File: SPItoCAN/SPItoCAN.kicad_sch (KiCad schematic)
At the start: 16 parts, among them J1 CONN_01x02, J2 CONN_01x02, J3 CONN_01x02, J4 Conn_01x07, U1 TJA1051T-E, U2 MCP2515-xSO, Y1 Crystal_8MHz

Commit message: Cleaned up PCB layout, added ground plane
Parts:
- added TP1, TP10, TP11, TP12, TP13, TP2, TP3, TP4, TP5, TP6, TP7, TP8, TP9: Test_Point_SMD, TestPoint:TestPoint_Pad_D1.5mm, symbol baja_schematics:Test_Point_SMD
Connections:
- net CANH: now also TP2.1
- net CANL: now also TP1.1
- net CS: now also TP10.1
- net GND: now also C3.2, C4.2, C5.2, D1.1 (K), TP13.1
- net INT: now also TP5.1
- net RXCAN: now also TP4.1
- net SCK: now also TP8.1
- net SI: now also TP9.1
- net SO: now also TP11.1
- net TXCAN: now also TP3.1
- net VCC: now also TP12.1; no longer C3.2, C4.2, C5.2, D1.1 (K)
- net OSC1 renamed OSC+
- net OSC+: now also TP7.1
- net OSC2 renamed OSC-
- net OSC-: now also TP6.1

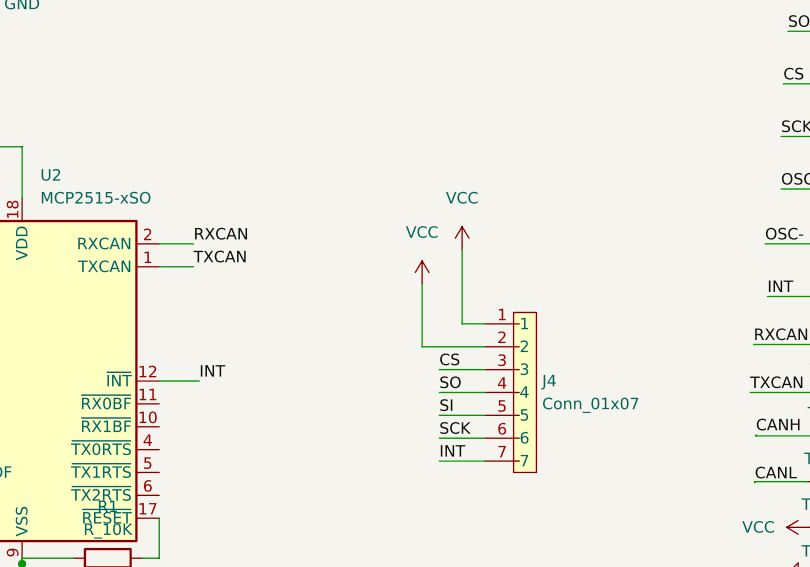
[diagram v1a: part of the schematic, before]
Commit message: cleaned up pcb, improved silkscreen, ran test gerber export
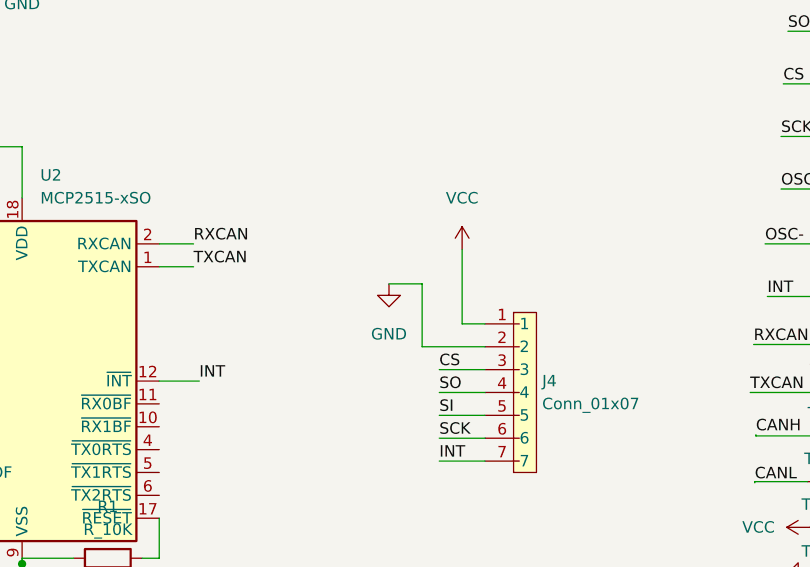
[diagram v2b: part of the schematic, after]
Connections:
- net GND: now also J4.2
- net VCC: no longer J4.2
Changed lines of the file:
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@@
+    (stroke (width 0) (type default) (color 0 0 0 0))
+  )
+  (wire (pts (xy 113.157 83.185) (xy 116.84 83.185))
     (stroke (width 0) (type default) (color 0 0 0 0))
   )
@@
     (pin "1")
   )
-  (symbol (lib_id "power:VCC") (at 116.84 83.185 0) (unit 1)
-    (in_bom yes) (on_board yes) (fields_autoplaced)
-    (property "Reference" "#PWR0104" (id 0) (at 116.84 86.995 0)
-      (effects (font (size 1.27 1.27)) hide)
-    )
-    (property "Value" "VCC" (id 1) (at 116.84 77.47 0))
-    (property "Footprint" "" (id 2) (at 116.84 83.185 0)
-      (effects (font (size 1.27 1.27)) hide)
-    )
-    (property "Datasheet" "" (id 3) (at 116.84 83.185 0)
-      (effects (font (size 1.27 1.27)) hide)
-    )
-    (pin "1")
-  )
   (symbol (lib_id "power:VCC") (at 67.945 119.38 0) (unit 1)
     (in_bom yes) (on_board yes)
@@
     )
     (property "Datasheet" "" (id 3) (at 161.29 100.076 0)
+      (effects (font (size 1.27 1.27)) hide)
+    )
+    (pin "1")
+  )
+  (symbol (lib_id "power:GND") (at 113.157 83.185 0) (unit 1)
+    (in_bom yes) (on_board yes) (fields_autoplaced)
+    (property "Reference" "#PWR0104" (id 0) (at 113.157 89.535 0)
+      (effects (font (size 1.27 1.27)) hide)
+    )
+    (property "Value" "GND" (id 1) (at 113.157 88.773 0))
+    (property "Footprint" "" (id 2) (at 113.157 83.185 0)
+      (effects (font (size 1.27 1.27)) hide)
+    )
+    (property "Datasheet" "" (id 3) (at 113.157 83.185 0)
       (effects (font (size 1.27 1.27)) hide)
     )
@@
       (reference "#PWR0103") (unit 1) (value "VCC") (footprint "")
     )
-    (path "/49441612-08d3-4f3e-a0e3-e44a83005088"
-      (reference "#PWR0104") (unit 1) (value "VCC") (footprint "")
+    (path "/7b13cfce-7857-47fb-8497-9e34fe39cc9c"
+      (reference "#PWR0104") (unit 1) (value "GND") (footprint "")
     )
     (path "/97c46783-6240-4233-9319-22c43f9f5727"

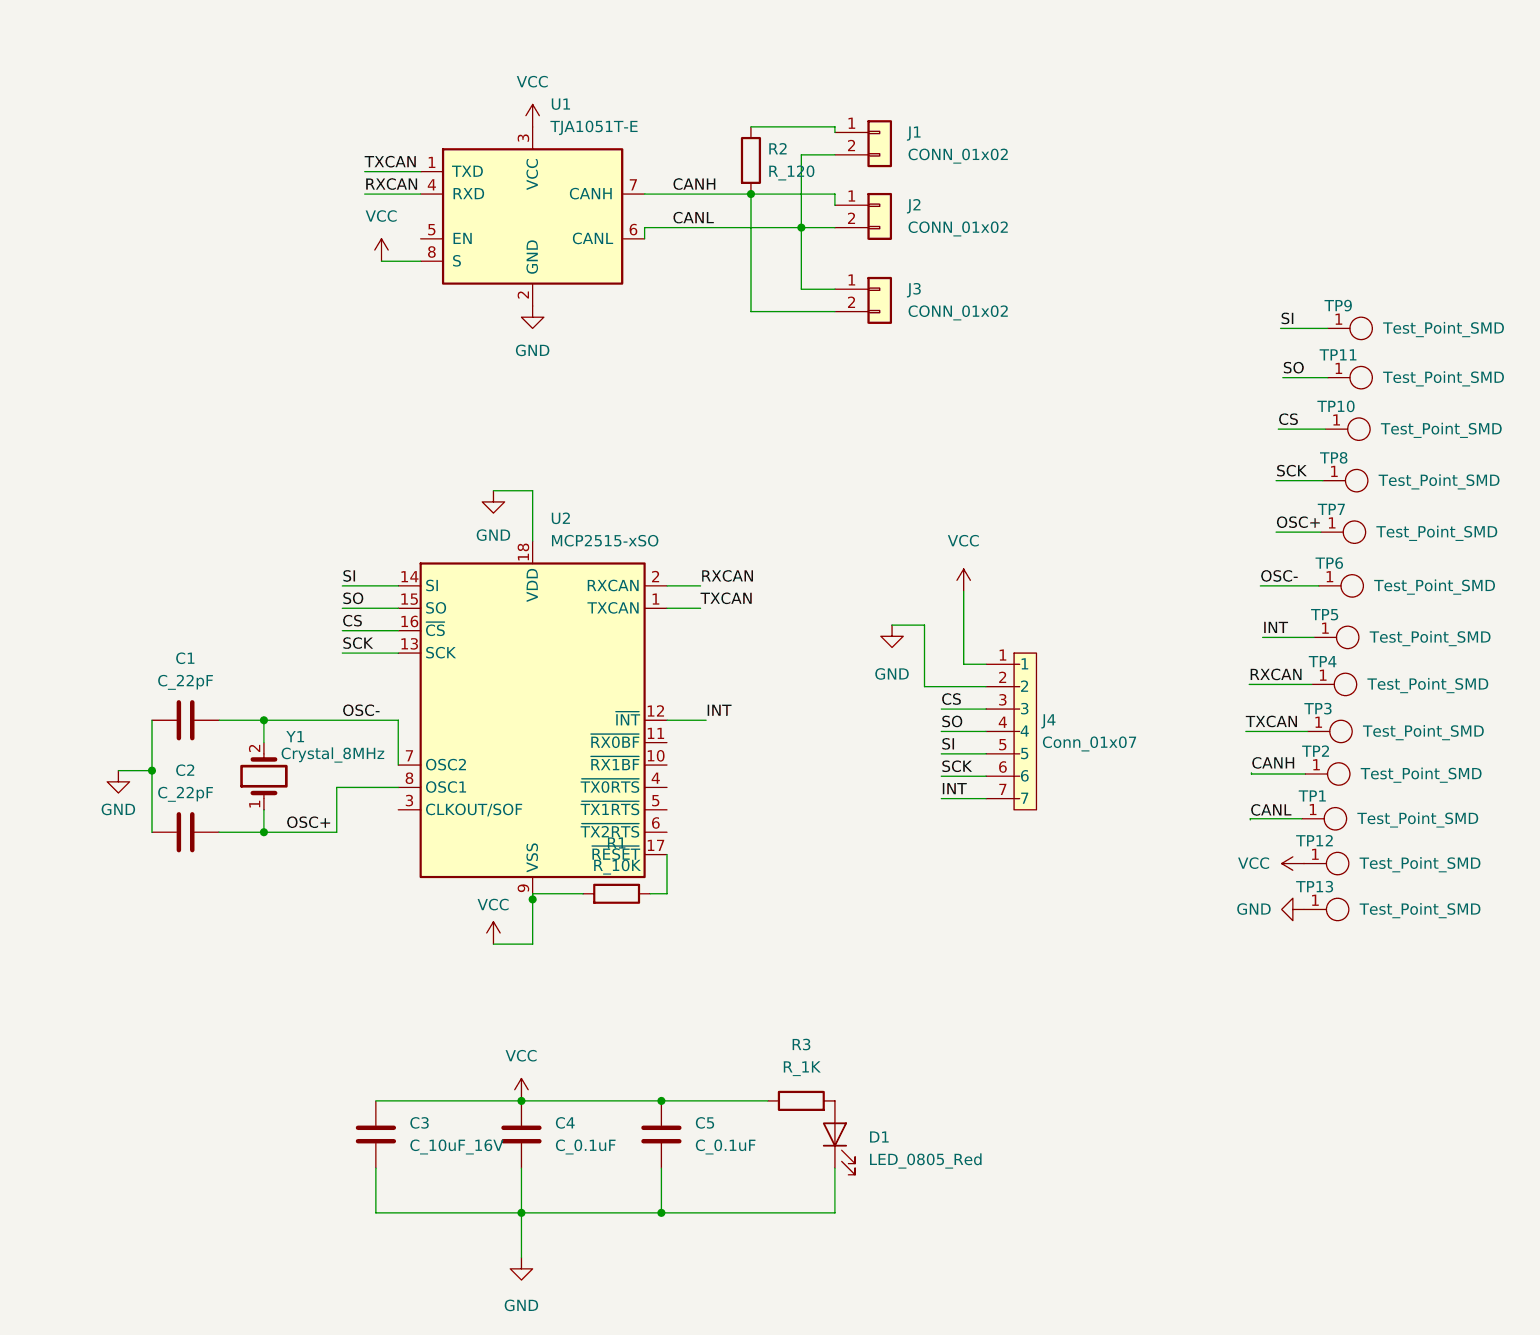
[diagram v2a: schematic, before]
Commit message: cleaned up layout; replaced LED; generated BOM
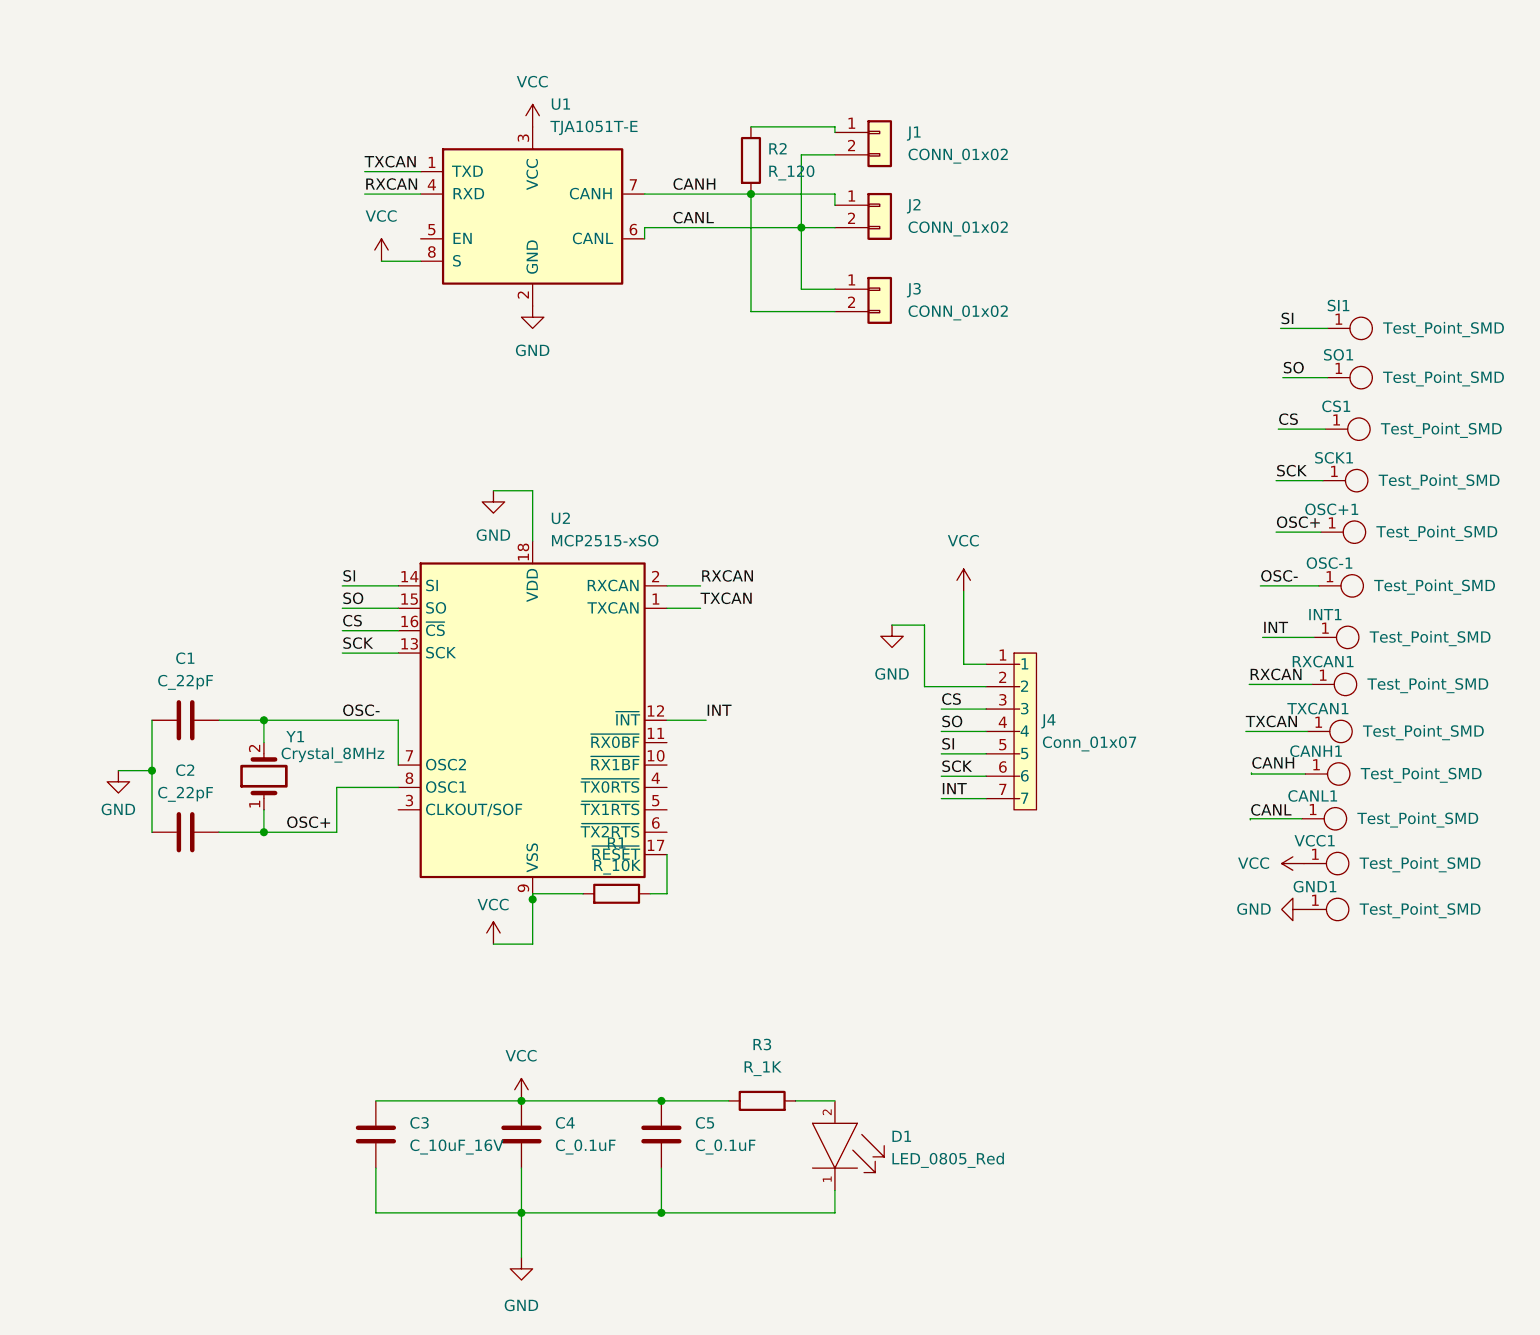
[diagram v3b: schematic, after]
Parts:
- D1: footprint footprints:LED_0805_OEM -> Baja:LED_0805_Red; Digikey PN (none) -> 516-1428-1-ND; MFN DK -> Avago; MPN 475-1415-1-ND -> HSMC-C170
- J4: PurchasingLink (none) -> https://www.digikey.com/en/products/detail/61300711121/732-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
- U2: symbol Interface_CAN_LIN:MCP2515-xSO -> baja_schematics:MCP2515-xSO; Digikey PN (none) -> MCP2515T-I/SODKR-ND; MPN (none) -> MCP2515T-I/SO; Purchasing Link (none) -> https://www.digikey.com/en/products/detail/microchip-techno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; PurchasingLink (none) -> https://www.digikey.com/en/products/detail/microchip-techno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
- renumbered TP2 to CANH1, TP1 to CANL1, TP10 to CS1, TP13 to GND1, TP5 to INT1, TP7 to OSC+1, TP6 to OSC-1, TP4 to RXCAN1, TP8 to SCK1, TP9 to SI1, TP11 to SO1, TP3 to TXCAN1, TP12 to VCC1
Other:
- moved on the sheet: R3

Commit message: Fixed some wiring & routing across the board; added explanatory notes to schematic
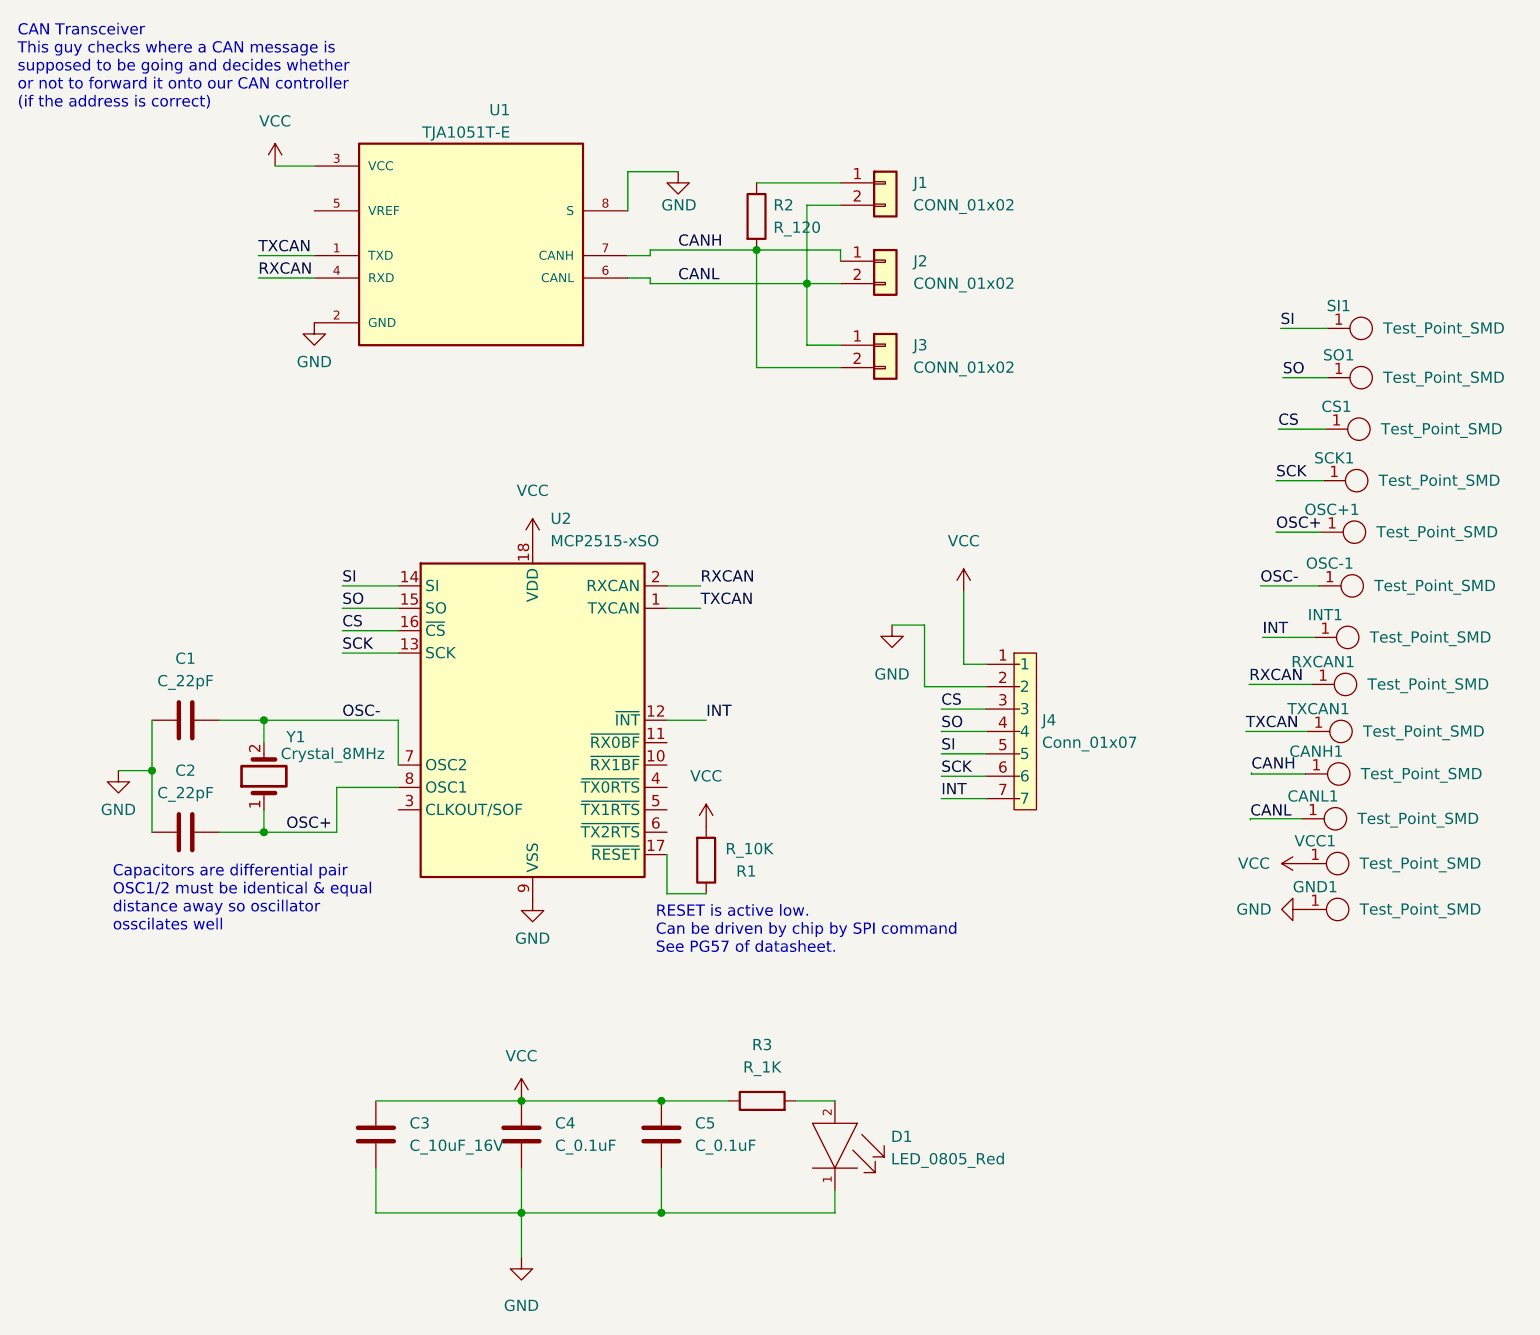
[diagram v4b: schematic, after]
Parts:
- U1: footprint Package_SO:SOIC-8_3.9x4.9mm_P1.27mm -> SOIC127P600X175-8N; symbol Interface_CAN_LIN:TJA1051T-E -> baja_schematics:TJA1050T; MANUFACTURER (none) -> NXP USA; MPN (none) -> TJA1050T/CM,118; PurchasingLink (none) -> https://www.mouser.com/ProductDetail/NXP-Semiconductors/TJA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; STANDARD (none) -> IPC 7351B
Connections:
- net GND: now also U1.8 (S), U2.9 (VSS); no longer U2.18 (VDD)
- net VCC: now also U2.18 (VDD); no longer U1.8 (S), U2.9 (VSS)
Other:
- note added: "CAN Transceiver This guy checks where a CAN message is supposed to be going and decides whether or not to forward it onto our CAN controller (if the address is correct)"
- note added: "Capacitors are differential pair OSC1/2 must be identical & equal distance away so oscillator osscilates well"
- note added: "RESET is active low. Can be driven by chip by SPI command See PG57 of datasheet."
- moved on the sheet: J1, J2, J3, R1, R2, U1
